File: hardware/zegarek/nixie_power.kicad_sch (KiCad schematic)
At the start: 14 parts, among them J1 Conn_01x02_Socket, J2 Conn_01x02_Pin, Q1 IRF740, U1 MC34063AD

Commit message: added doc and sink in pcb
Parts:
- J1: footprint Connector_PinHeader_2.54mm:PinHeader_1x02_P2.54mm_Vertical -> Connector:Banana_Jack_2Pin
- J2: footprint Connector_Phoenix_MC_HighVoltage:PhoenixContact_MCV_1,5_2-G-5.08_1x02_P5.08mm_Vertical -> Connector:Banana_Jack_2Pin
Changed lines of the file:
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@@
 			)
 		)
-		(property "Footprint" "Connector_Phoenix_MC_HighVoltage:PhoenixContact_MCV_1,5_2-G-5.08_1x02_P5.08mm_Vertical"
+		(property "Footprint" "Connector:Banana_Jack_2Pin"
 			(at 265.43 35.56 0)
 			(effects
@@
 			)
 		)
-		(property "Footprint" "Connector_PinHeader_2.54mm:PinHeader_1x02_P2.54mm_Vertical"
+		(property "Footprint" "Connector:Banana_Jack_2Pin"
 			(at 30.48 36.83 0)
 			(effects

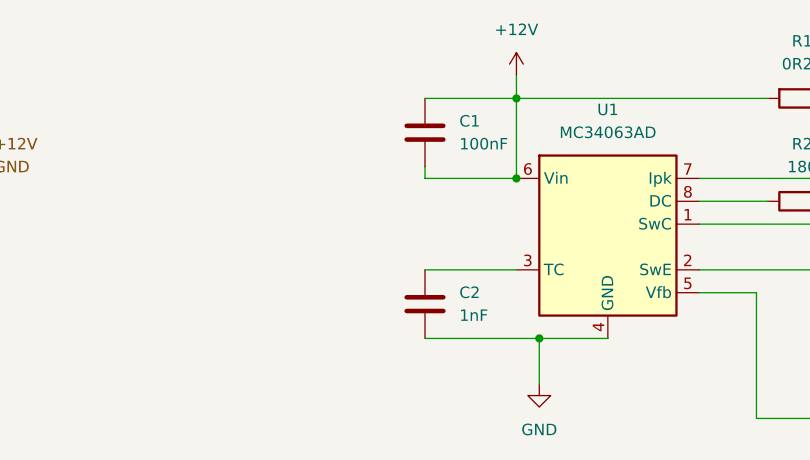
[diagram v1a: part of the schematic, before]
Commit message: c1 pwr/gnd
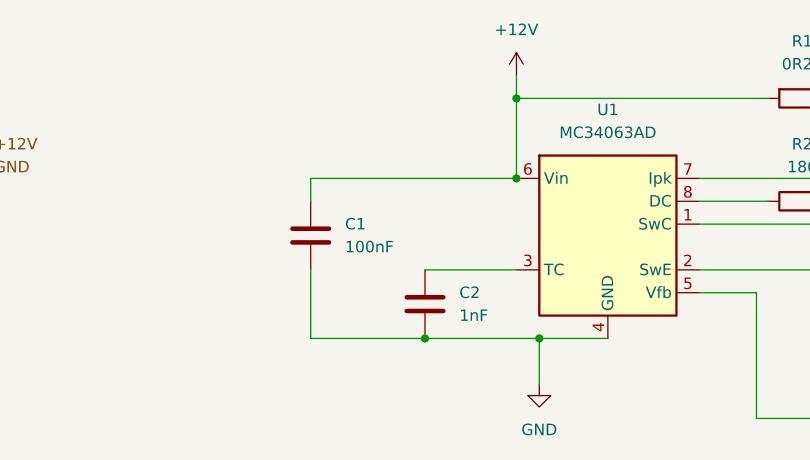
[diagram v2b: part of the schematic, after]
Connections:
- net +12V: no longer C1.1
- net GND: now also C1.1
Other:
- moved on the sheet: C1
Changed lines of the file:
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@@
+	)
+	(junction
+		(at 97.79 55.88)
+		(diameter 0)
+		(color 0 0 0 0)
 	)
 	(junction
@@
 	(wire
 		(pts
-			(xy 97.79 29.21) (xy 107.95 29.21)
-		)
-		(stroke
-			(width 0)
-			(type default)
-		)
-	)
-	(wire
-		(pts
 			(xy 190.5 55.88) (xy 199.39 55.88)
 		)
@@
 	(wire
 		(pts
-			(xy 97.79 38.1) (xy 107.95 38.1)
+			(xy 85.09 38.1) (xy 107.95 38.1)
+		)
+		(stroke
+			(width 0)
+			(type default)
+		)
+	)
+	(wire
+		(pts
+			(xy 85.09 48.26) (xy 85.09 55.88)
 		)
 		(stroke
@@
 	(wire
 		(pts
+			(xy 85.09 55.88) (xy 97.79 55.88)
+		)
+		(stroke
+			(width 0)
+			(type default)
+		)
+	)
+	(wire
+		(pts
 			(xy 246.38 33.02) (xy 254 33.02)
 		)
@@
 	(wire
 		(pts
-			(xy 97.79 36.83) (xy 97.79 38.1)
+			(xy 85.09 38.1) (xy 85.09 40.64)
 		)
 		(stroke
@@
 	(symbol
 		(lib_id "Device:C")
-		(at 97.79 33.02 0)
+		(at 85.09 44.45 180)
 		(unit 1)
 		(exclude_from_sim no)
@@
 		(fields_autoplaced yes)
 		(property "Reference" "C1"
-			(at 101.6 31.7499 0)
-			(effects
-				(font
-					(size 1.27 1.27)
-				)
-				(justify left)
+			(at 88.9 43.1799 0)
+			(effects
+				(font
+					(size 1.27 1.27)
+				)
+				(justify right)
 			)
 		)
 		(property "Value" "100nF"
-			(at 101.6 34.2899 0)
-			(effects
-				(font
-					(size 1.27 1.27)
-				)
-				(justify left)
+			(at 88.9 45.7199 0)
+			(effects
+				(font
+					(size 1.27 1.27)
+				)
+				(justify right)
 			)
 		)
 		(property "Footprint" "Capacitor_SMD:C_1206_3216Metric_Pad1.33x1.80mm_HandSolder"
-			(at 98.7552 36.83 0)
+			(at 84.1248 40.64 0)
 			(effects
 				(font
@@
 		)
 		(property "Datasheet" "~"
-			(at 97.79 33.02 0)
+			(at 85.09 44.45 0)
 			(effects
 				(font
@@
 		)
 		(property "Description" "Unpolarized capacitor"
-			(at 97.79 33.02 0)
-			(effects
-				(font
+			(at 85.09 44.45 0)
+			(effects
+				(font

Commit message: diode correction
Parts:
- D1: value UF5400 -> UF4007
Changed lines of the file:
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@@
 			)
 		)
-		(property "Value" "UF5400"
+		(property "Value" "UF4007"
 			(at 179.07 31.75 0)
 			(effects
